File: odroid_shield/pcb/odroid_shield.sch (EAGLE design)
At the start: 68 parts, among them J1 AVRISP6_COMPACT, J4 ODROID_J4, U1 SINGLE-BIT_BUS_TRANSCEIVER, U10 ABM8G, U2 SINGLE-BIT_BUS_TRANSCEIVER, U3 ST1S10, U4 ATMEGA644P-20AU, U5 TS5205, U6 TCA9517MSOP8, U7 MP33926, U8 MAX21000, U9 MMA8451Q

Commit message: odroid_shield: Run schematic ERC.
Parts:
- added C16, C17: .1uF, rcl:C-USC0603
- ARM: value (none) -> FLASH_RED
- D1, D2: value (none) -> 30V 2A
- IND: value (none) -> RED
- PWR: value (none) -> GREEN
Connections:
- new net N$30: C16.1, U4.AREF
- net +5V: now also C17.1
- net GND: now also C16.2, C17.2
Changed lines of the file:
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@@
 <part name="B-" library="odroid_shield" deviceset="BAT_TERM" device=""/>
 <part name="GND4" library="supply1" deviceset="GND" device=""/>
-<part name="ARM" library="led" deviceset="LED" device="5MM">
+<part name="ARM" library="led" deviceset="LED" device="5MM" value="FLASH_RED">
 <attribute name="DPN" value="67-1499-ND"/>
 </part>
-<part name="PWR" library="led" deviceset="LED" device="CHIPLED_0805"/>
+<part name="PWR" library="led" deviceset="LED" device="CHIPLED_0805" value="GREEN"/>
 <part name="SHORE" library="odroid_shield" deviceset="PJ-034A" device="SMT" value="PJ-034ASMT">
 <attribute name="DPN" value="CP-015AHPJ-CT-ND"/>
@@
 <attribute name="DPN" value="399-7847-1-ND"/>
 </part>
-<part name="D1" library="odroid_shield" deviceset="DIODE-" device="CMS06">
+<part name="D1" library="odroid_shield" deviceset="DIODE-" device="CMS06" value="30V 2A">
 <attribute name="DPN" value="CMS06QMCT-ND"/>
 </part>
-<part name="D2" library="odroid_shield" deviceset="DIODE-" device="CMS06">
+<part name="D2" library="odroid_shield" deviceset="DIODE-" device="CMS06" value="30V 2A">
 <attribute name="DPN" value="CMS06QMCT-ND"/>
 </part>
@@
 <part name="P+8" library="supply1" deviceset="+5V" device=""/>
 <part name="GND11" library="supply1" deviceset="GND" device=""/>
-<part name="IND" library="led" deviceset="LED" device="CHIPLED_0805"/>
+<part name="IND" library="led" deviceset="LED" device="CHIPLED_0805" value="RED"/>
 <part name="SER2" library="pinhead" deviceset="PINHD-1X4" device="">
 <attribute name="DPN" value="S9410-ND"/>
@@
 <part name="C14" library="rcl" deviceset="C-US" device="C0603" value=".1uF"/>
 <part name="C15" library="rcl" deviceset="C-US" device="C0603" value=".1uF"/>
+<part name="C16" library="rcl" deviceset="C-US" device="C0603" value=".1uF"/>
+<part name="GND17" library="supply1" deviceset="GND" device=""/>
+<part name="C17" library="rcl" deviceset="C-US" device="C0603" value=".1uF"/>
+<part name="GND18" library="supply1" deviceset="GND" device=""/>
 </parts>
 <sheets>
@@
 <instance part="U4" gate="A" x="86.36" y="294.64"/>
 <instance part="GND10" gate="1" x="78.74" y="228.6"/>
-<instance part="P+7" gate="1" x="58.42" y="347.98"/>
+<instance part="P+7" gate="1" x="58.42" y="353.06"/>
 <instance part="J1" gate="A" x="12.7" y="292.1"/>
 <instance part="P+8" gate="1" x="-7.62" y="314.96"/>
@@
 <instance part="C14" gate="G$1" x="142.24" y="393.7"/>
 <instance part="C15" gate="G$1" x="152.4" y="393.7"/>
+<instance part="C16" gate="G$1" x="55.88" y="307.34"/>
+<instance part="GND17" gate="1" x="55.88" y="299.72"/>
+<instance part="C17" gate="G$1" x="50.8" y="335.28"/>
+<instance part="GND18" gate="1" x="50.8" y="327.66"/>
 </instances>
 <busses>
@@
 <segment>
 <pinref part="P+7" gate="1" pin="+5V"/>
-<wire x1="58.42" y1="345.44" x2="58.42" y2="330.2" width="0.1524" layer="91"/>
+<wire x1="58.42" y1="350.52" x2="58.42" y2="342.9" width="0.1524" layer="91"/>
 <pinref part="U4" gate="A" pin="VCC_2"/>
+<wire x1="58.42" y1="342.9" x2="58.42" y2="330.2" width="0.1524" layer="91"/>
 <wire x1="58.42" y1="330.2" x2="68.58" y2="330.2" width="0.1524" layer="91"/>
 <wire x1="58.42" y1="330.2" x2="58.42" y2="327.66" width="0.1524" layer="91"/>
@@
 <pinref part="U4" gate="A" pin="AVCC"/>
 <wire x1="58.42" y1="322.58" x2="68.58" y2="322.58" width="0.1524" layer="91"/>
+<pinref part="C17" gate="G$1" pin="1"/>
+<wire x1="50.8" y1="337.82" x2="50.8" y2="342.9" width="0.1524" layer="91"/>
+<wire x1="58.42" y1="342.9" x2="50.8" y2="342.9" width="0.1524" layer="91"/>
+<junction x="58.42" y="342.9"/>
 </segment>
 <segment>
@@
 <junction x="152.4" y="381"/>
 </segment>
+<segment>
+<pinref part="C16" gate="G$1" pin="2"/>
+<pinref part="GND17" gate="1" pin="GND"/>
+</segment>
+<segment>
+<pinref part="C17" gate="G$1" pin="2"/>
+<pinref part="GND18" gate="1" pin="GND"/>
+</segment>
 </net>
 <net name="N$2" class="0">
@@
 <pinref part="U10" gate="G$1" pin="OSC@3"/>
 <wire x1="137.16" y1="358.14" x2="116.84" y2="358.14" width="0.1524" layer="91"/>
-<wire x1="116.84" y1="358.14" x2="45.72" y2="358.14" width="0.1524" layer="91"/>
-<wire x1="45.72" y1="358.14" x2="45.72" y2="317.5" width="0.1524" layer="91"/>
+<wire x1="116.84" y1="358.14" x2="33.02" y2="358.14" width="0.1524" layer="91"/>
+<wire x1="33.02" y1="358.14" x2="33.02" y2="317.5" width="0.1524" layer="91"/>
 <pinref part="U4" gate="A" pin="XTAL1"/>
-<wire x1="45.72" y1="317.5" x2="68.58" y2="317.5" width="0.1524" layer="91"/>
+<wire x1="33.02" y1="317.5" x2="68.58" y2="317.5" width="0.1524" layer="91"/>
 <pinref part="C11" gate="G$1" pin="1"/>
 <wire x1="116.84" y1="347.98" x2="116.84" y2="358.14" width="0.1524" layer="91"/>
@@
 </segment>
 </net>
+<net name="N$30" class="0">
+<segment>
+<pinref part="C16" gate="G$1" pin="1"/>
+<pinref part="U4" gate="A" pin="AREF"/>
+<wire x1="55.88" y1="309.88" x2="68.58" y2="309.88" width="0.1524" layer="91"/>
+</segment>
+</net>
 </nets>
 </sheet>
 </sheets>
+<errors>
+</errors>
 </schematic>
 </drawing>

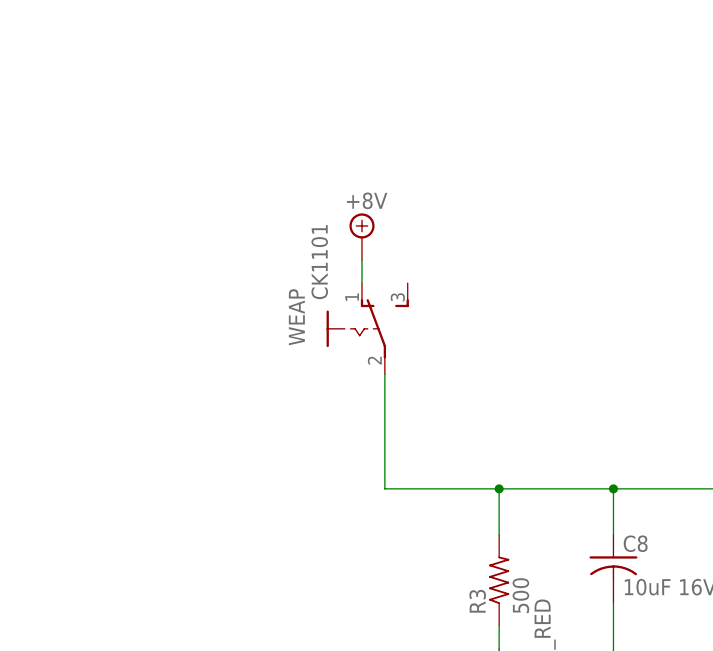
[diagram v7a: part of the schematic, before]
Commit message: odroid_shield: Manually routed servo data lines and other tweaks to improve overall routability.
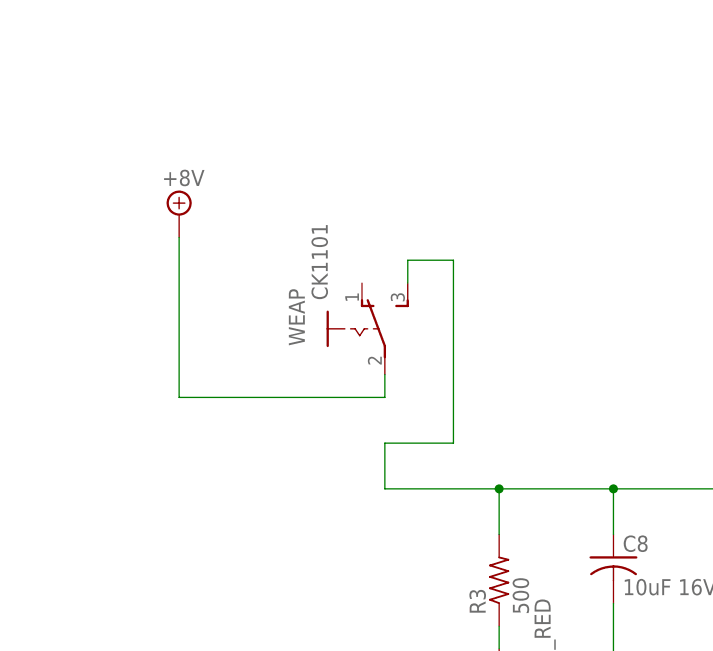
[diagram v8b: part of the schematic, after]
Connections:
- net +8V: now also WEAP.P; no longer WEAP.O
- net N$15: now also WEAP.S; no longer WEAP.P
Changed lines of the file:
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@@
 <instance part="GND7" gate="1" x="132.08" y="106.68"/>
 <instance part="GND8" gate="1" x="203.2" y="134.62"/>
-<instance part="SUPPLY3" gate="+8V" x="25.4" y="193.04"/>
+<instance part="SUPPLY3" gate="+8V" x="5.08" y="195.58"/>
 <instance part="C7" gate="G$1" x="68.58" y="157.48"/>
 <instance part="C8" gate="G$1" x="53.34" y="157.48">
@@
 <segment>
 <pinref part="SUPPLY3" gate="+8V" pin="+8V"/>
-<pinref part="WEAP" gate="G$1" pin="O"/>
-<wire x1="25.4" y1="190.5" x2="25.4" y2="187.96" width="0.1524" layer="91"/>
+<wire x1="5.08" y1="193.04" x2="5.08" y2="175.26" width="0.1524" layer="91"/>
+<pinref part="WEAP" gate="G$1" pin="P"/>
+<wire x1="5.08" y1="175.26" x2="27.94" y2="175.26" width="0.1524" layer="91"/>
+<wire x1="27.94" y1="175.26" x2="27.94" y2="177.8" width="0.1524" layer="91"/>
 </segment>
 </net>
@@
 <net name="N$15" class="0">
 <segment>
-<pinref part="WEAP" gate="G$1" pin="P"/>
-<wire x1="27.94" y1="177.8" x2="27.94" y2="165.1" width="0.1524" layer="91"/>
 <wire x1="27.94" y1="165.1" x2="40.64" y2="165.1" width="0.1524" layer="91"/>
 <pinref part="C8" gate="G$1" pin="1"/>
@@
 <wire x1="139.7" y1="170.18" x2="139.7" y2="167.64" width="0.1524" layer="91"/>
 <junction x="132.08" y="170.18"/>
-</segment>
-</net>
+<wire x1="27.94" y1="165.1" x2="27.94" y2="170.18" width="0.1524" layer="91"/>
+<wire x1="27.94" y1="170.18" x2="35.56" y2="170.18" width="0.1524" layer="91"/>
+<wire x1="35.56" y1="170.18" x2="35.56" y2="190.5" width="0.1524" layer="91"/>
+<pinref part="WEAP" gate="G$1" pin="S"/>
+<wire x1="35.56" y1="190.5" x2="30.48" y2="190.5" width="0.1524" layer="91"/>
+<wire x1="30.48" y1="190.5" x2="30.48" y2="187.96" width="0.1524" layer="91"/>
+</segment>
+</net>
